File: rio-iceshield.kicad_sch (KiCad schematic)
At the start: 61 parts, among them J2 Conn_01x06, J3 Conn_01x06, J4 Conn_01x06, J5 Conn_01x06, J6 Conn_01x06, J7 Conn_02x06_Odd_Even, U1 ICE40UP5K-SG48ITR, U2 AT25SF041B-SHD 4 Mb, U3 LD3985M122R_SOT23, U9 ULN2803A, X2 XO91, j1 GPIO

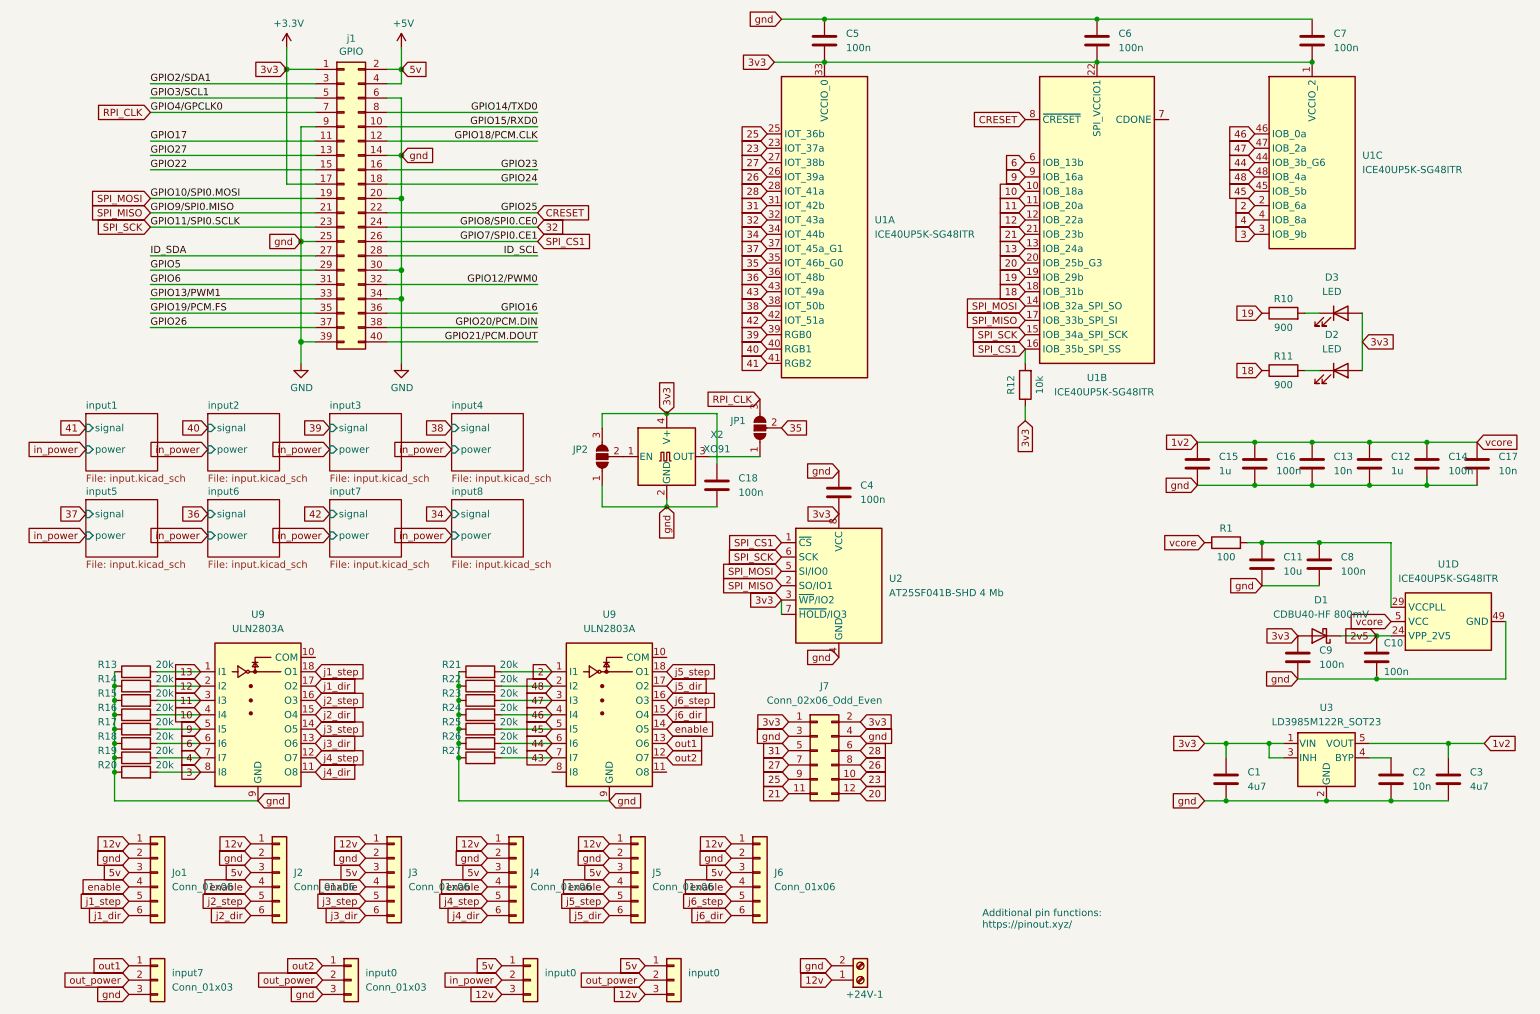
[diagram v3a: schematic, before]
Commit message: other diode (i used in on my test-board)
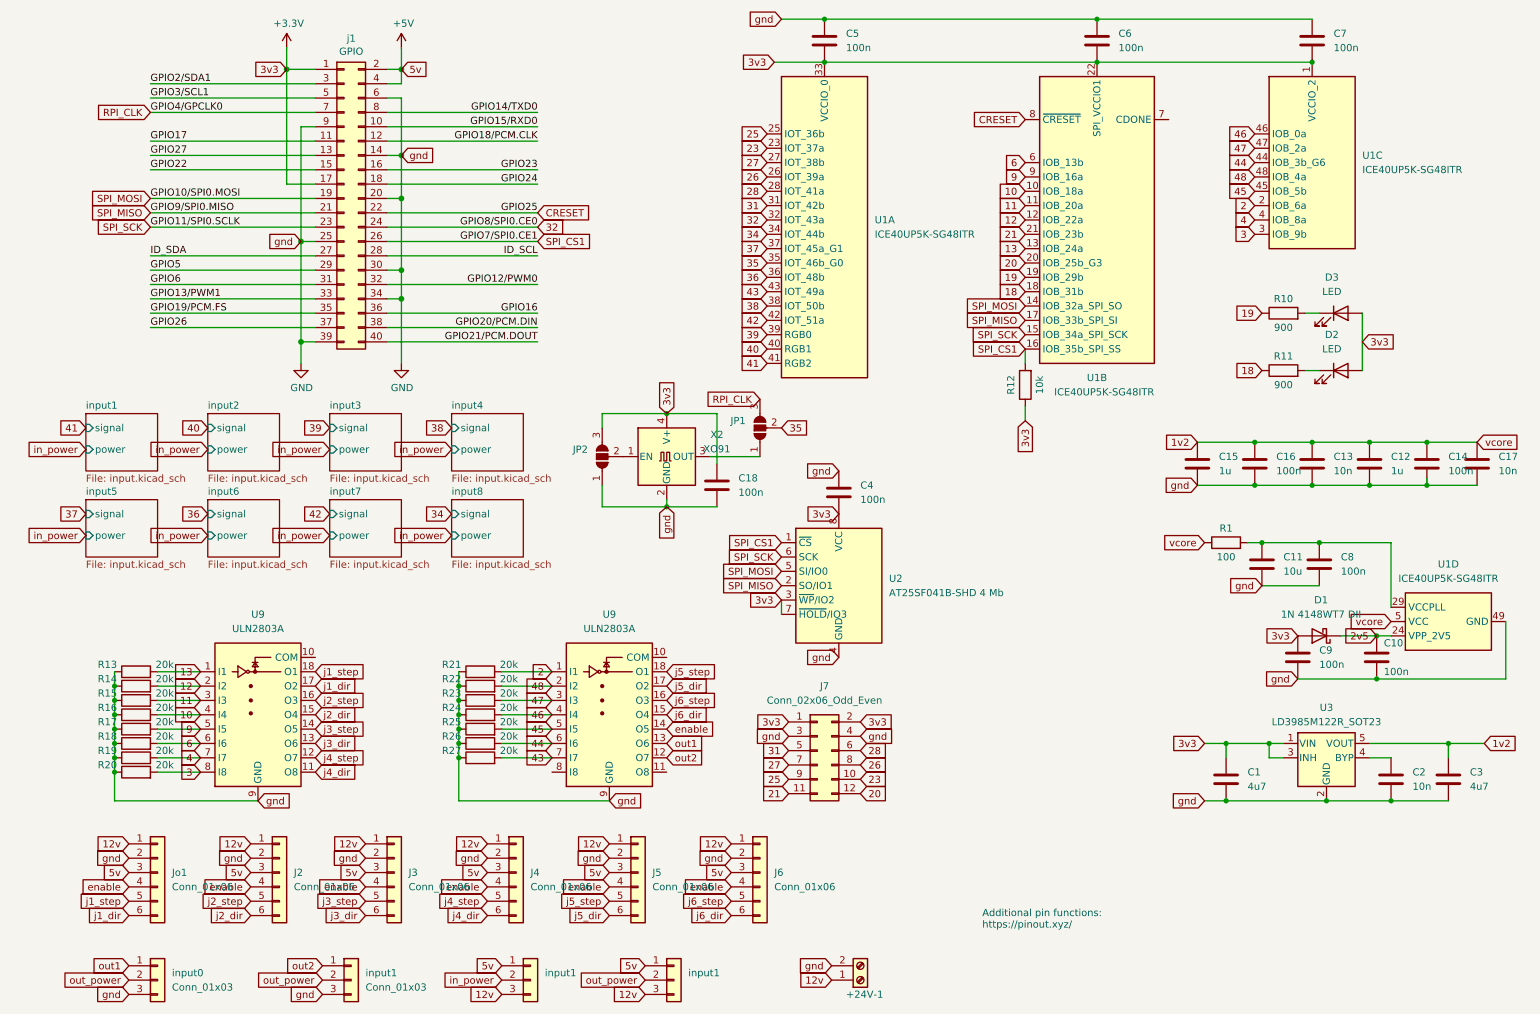
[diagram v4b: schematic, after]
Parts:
- D1: value CDBU40-HF 800mV -> 1N 4148WT7 DII
- renumbered input7 to input0, input0 to input1

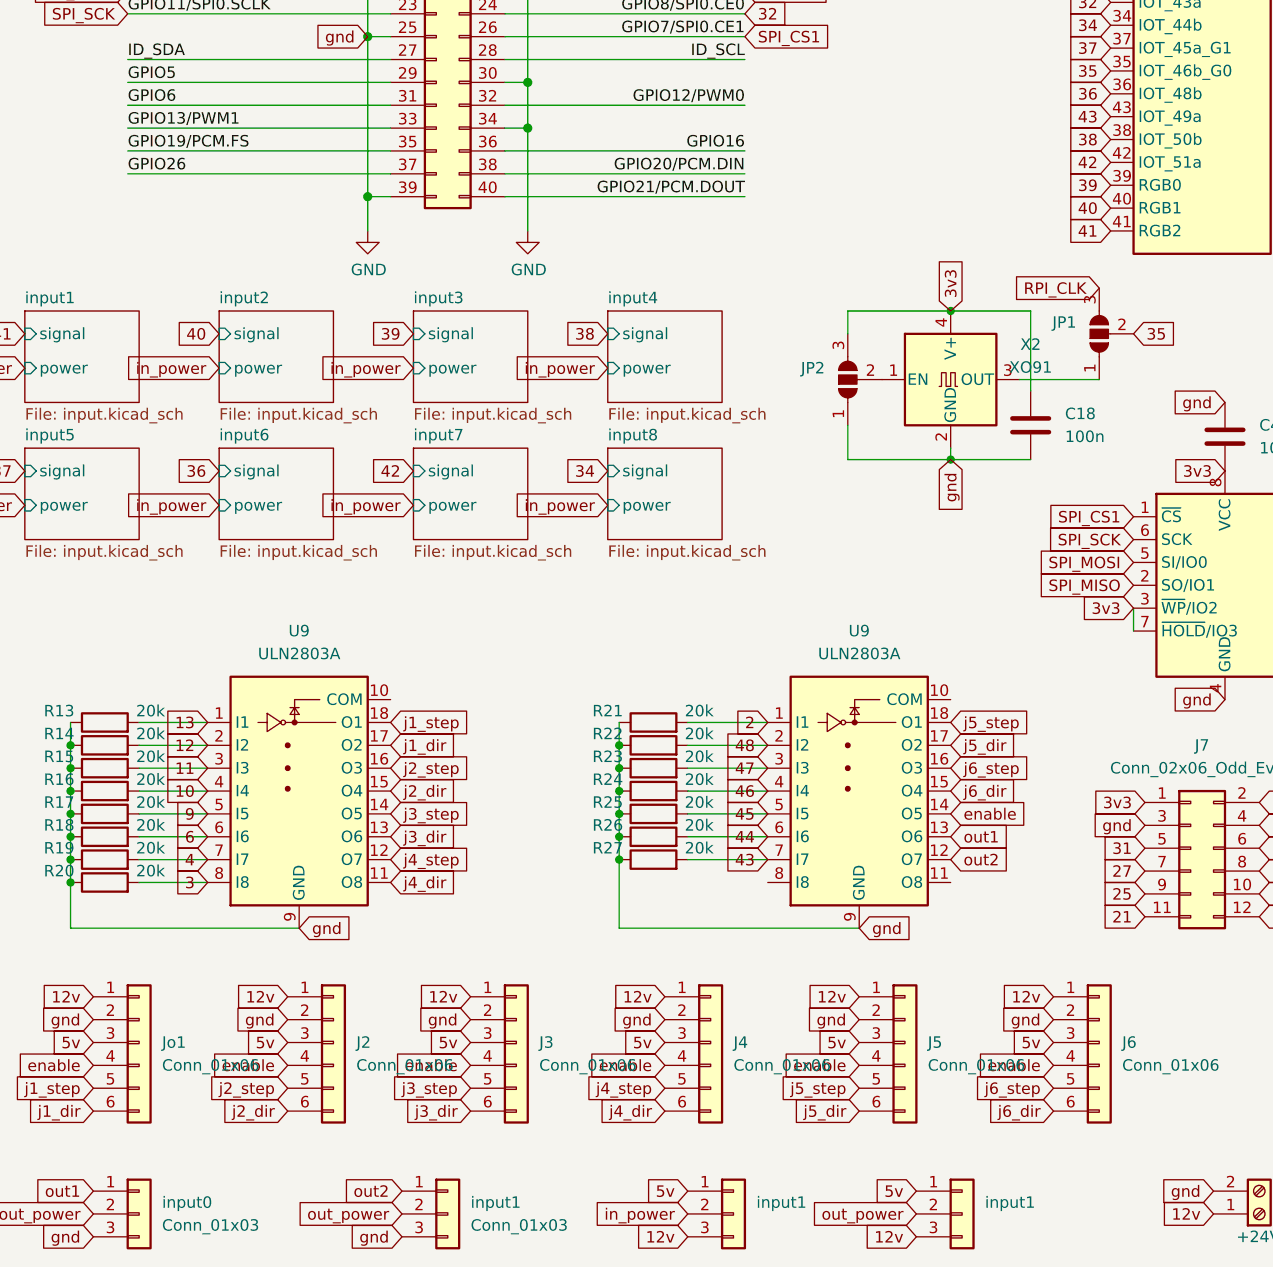
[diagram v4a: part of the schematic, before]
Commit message: adding pullups to in1-3
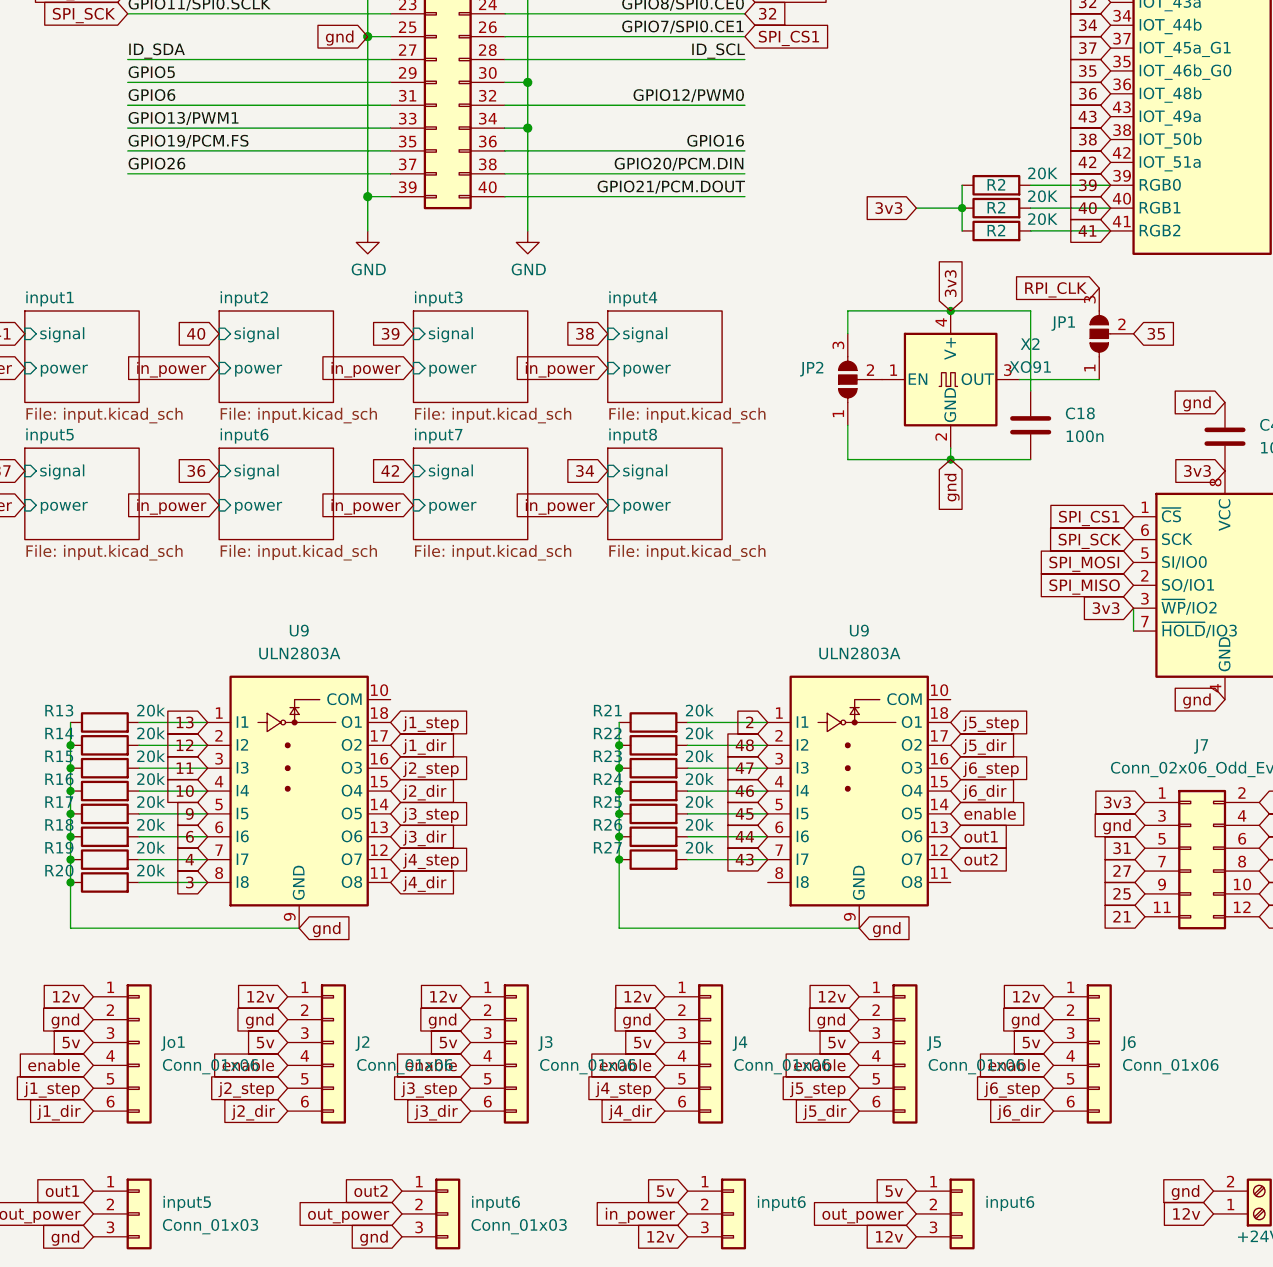
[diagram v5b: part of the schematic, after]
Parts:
- added R2 (x3): 20K, Resistor_SMD:R_1206_3216Metric, symbol Device:R
- renumbered input0 to input5, input1 to input6
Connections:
- net +3V3: now also R2.1, R2.1, R2.1
- net 39: now also R2.2
- net 40: now also R2.2
- net 41: now also R2.2

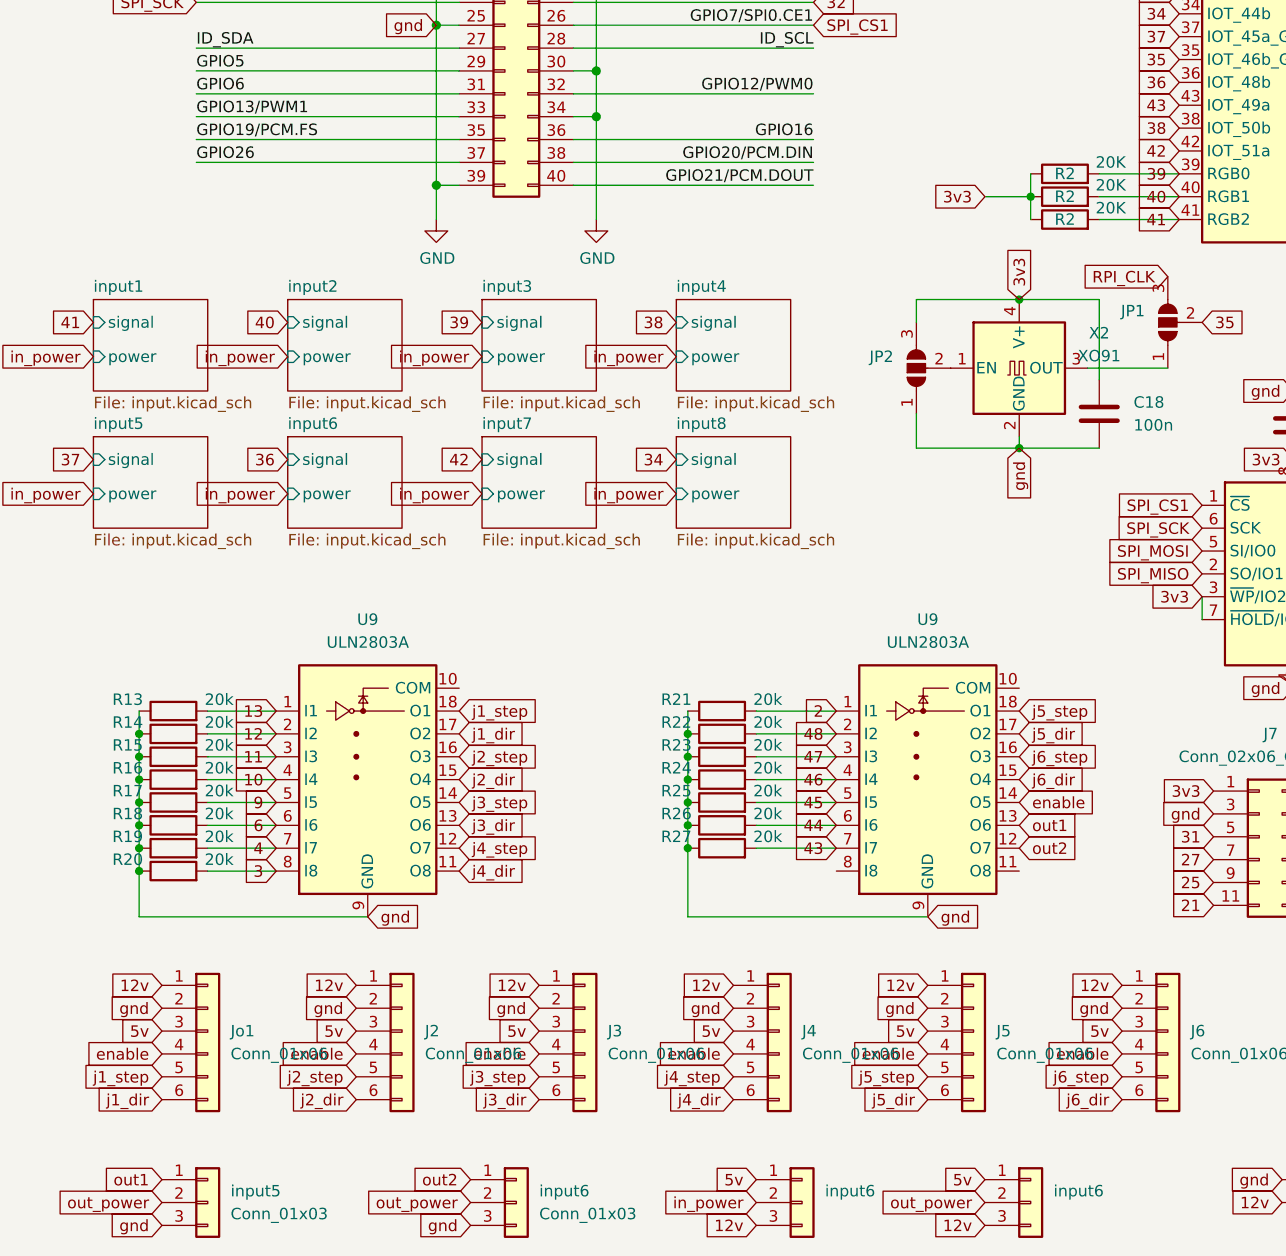
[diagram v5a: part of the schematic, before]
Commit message: adding pullups to out1-2
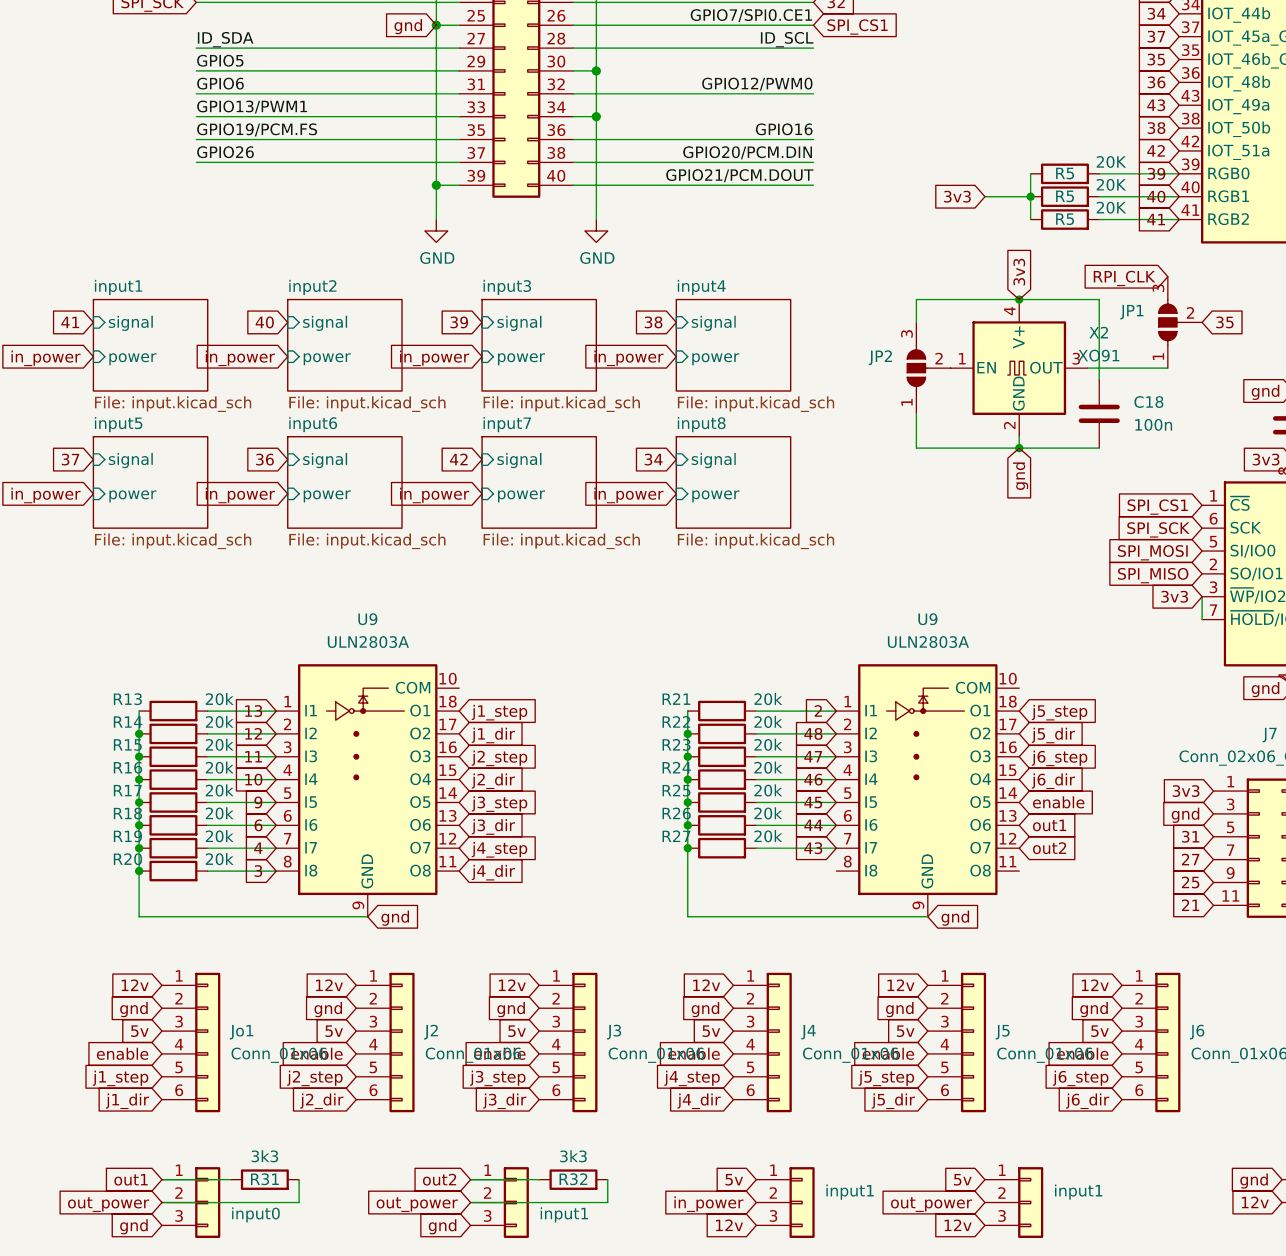
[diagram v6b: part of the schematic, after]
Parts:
- added R31, R32: 3k3, Resistor_SMD:R_0805_2012Metric_Pad1.20x1.40mm_HandSolder, symbol Device:R
- renumbered R2 to R5, input5 to input0, input6 to input1
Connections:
- net out1: now also R31.1
- net out2: now also R32.1
- net out_power: now also R31.2, R32.2
